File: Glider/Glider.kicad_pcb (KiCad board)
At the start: 2 copper layers, 100 x 200 mm, 3 parts

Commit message: Glider done !
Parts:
- removed H3: Panel, Kosmo_panel:Kosmo_Panel_Dual_Mounting_Holes
- added C1: 100n, Capacitor_THT:C_Disc_D7.0mm_W2.5mm_P5.00mm, F.Cu at (28.7, 115.4)
- added C2: 100n, Capacitor_THT:C_Disc_D7.0mm_W2.5mm_P5.00mm, F.Cu at (20.7, 125.2)
- added C3: 470n, Capacitor_THT:C_Disc_D7.0mm_W2.5mm_P5.00mm, F.Cu at (35.3, 47.9)
- added C4: 470n, Capacitor_THT:C_Disc_D7.0mm_W2.5mm_P5.00mm, F.Cu at (35.4, 144.1)
- added D1: LED, LED_SMD:LED_1206_3216Metric_ReverseMount_Hole1.8x2.4mm, B.Cu at (29.9, 91.2)
- added D2: 1N4148, Diode_THT:D_DO-35_SOD27_P7.62mm_Horizontal, F.Cu at (21.8, 51.9)
- added D3: 1N4148, Diode_THT:D_DO-35_SOD27_P7.62mm_Horizontal, F.Cu at (17.2, 49.1)
- added D4: LED, LED_SMD:LED_1206_3216Metric_ReverseMount_Hole1.8x2.4mm, B.Cu at (30.1, 185.4)
- added D5: 1N4148, Diode_THT:D_DO-35_SOD27_P7.62mm_Horizontal, F.Cu at (22.0, 148.3)
- added D6: 1N4148, Diode_THT:D_DO-35_SOD27_P7.62mm_Horizontal, F.Cu at (17.2, 145.6)
- added J1: EuroPower, telec:EuroPower, B.Cu at (29.7, 25.8)
- added J2: OUT1, telec:JackHole, F.Cu at (23.3, 101.9)
- added J3: IN1, telec:JackHole, F.Cu at (23.3, 80.9)
- added J4: OUT2, telec:JackHole, F.Cu at (23.3, 196.1)
- added J5: IN2, telec:JackHole, F.Cu at (23.3, 175.1)
- added LOGO1: telec, logo:telec-8, F.Cu at (25.0, 16.4)
- added R1: 2k2, Resistor_SMD:R_1206_3216Metric_Pad1.42x1.75mm_HandSolder, B.Cu at (32.8, 109.8)
- added R2: 1k, Resistor_THT:R_Axial_DIN0204_L3.6mm_D1.6mm_P7.62mm_Horizontal, F.Cu at (36.0, 93.0)
- added R3: 100, Resistor_THT:R_Axial_DIN0204_L3.6mm_D1.6mm_P7.62mm_Horizontal, F.Cu at (32.4, 53.2)
- added R4: 2k2, Resistor_SMD:R_1206_3216Metric_Pad1.42x1.75mm_HandSolder, B.Cu at (34.5, 182.9)
- added R5: 1k, Resistor_THT:R_Axial_DIN0204_L3.6mm_D1.6mm_P7.62mm_Horizontal, F.Cu at (36.0, 187.2)
- added R6: 100, Resistor_THT:R_Axial_DIN0204_L3.6mm_D1.6mm_P7.62mm_Horizontal, F.Cu at (32.7, 149.4)
- added RV1: 1M, Potentiometer_THT:Potentiometer_Alps_RK09K_Single_Vertical, F.Cu at (27.1, 45.6)
- added RV2: 1M, Potentiometer_THT:Potentiometer_Alps_RK09K_Single_Vertical, F.Cu at (27.1, 141.7)
- added SW1: LIN/LOG, telec:SW_L13.2mm_W7.9mm_P4.7mm, F.Cu at (32.3, 61.5)
- added SW2: UP/DOWN, telec:SW_L13.2mm_W7.9mm_P4.7mm, F.Cu at (16.9, 61.6)
- added SW3: LIN/LOG, telec:SW_L13.2mm_W7.9mm_P4.7mm, F.Cu at (32.1, 157.7)
- added SW4: UP/DOWN, telec:SW_L13.2mm_W7.9mm_P4.7mm, F.Cu at (17.0, 157.7)
- added U1: TL082, Package_DIP:DIP-8_W7.62mm_LongPads, F.Cu at (14.5, 114.3)
- added U2: TL082, Package_DIP:DIP-8_W7.62mm_LongPads, F.Cu at (27.2, 118.7)
- H1, H2: value Panel -> Mounting_Holes
- moved H2 47.6 mm to (15.1, 209.1)
- moved H1 19.0 mm to (34.1, 209.1)
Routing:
- net -12V: track 0.00 -> 132.7 mm
- net +12V: track 0.00 -> 132.7 mm
- net Net-(C3-Pad2): track 0.00 -> 109.2 mm
- net Net-(R3-Pad1): track 0.00 -> 75.0 mm
- net Net-(J4-PadT): track 0.00 -> 71.7 mm, vias 0 -> 1
- net /OUT2: track 0.00 -> 69.4 mm, vias 0 -> 1
- net Net-(SW1-Pad2): track 0.00 -> 68.9 mm
- net /IN1: track 0.00 -> 66.8 mm
- net Net-(C4-Pad2): track 0.00 -> 58.2 mm
- net /IN2: track 0.00 -> 51.7 mm
- net Net-(R6-Pad1): track 0.00 -> 50.7 mm
- net Net-(SW3-Pad2): track 0.00 -> 46.6 mm
- net Net-(J2-PadT): track 0.00 -> 38.9 mm
- net Net-(R6-Pad2): track 0.00 -> 30.2 mm
- net Net-(R3-Pad2): track 0.00 -> 30.1 mm
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- added copper zone on B.Cu, net GND
- added copper zone on F.Cu, net GND
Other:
- board size 100 x 200 mm -> 25 x 200 mm
- board text added: "+12V"
- board text added: "-12V"
- board text added: "DOWN"
- board text added: "Dual CV Glider"
- board text added: "From Harald Antes schematic, from Ives Uson"
- board text added: "GND"
- board text added: "LIN/LOG"
- board text added: "UP"

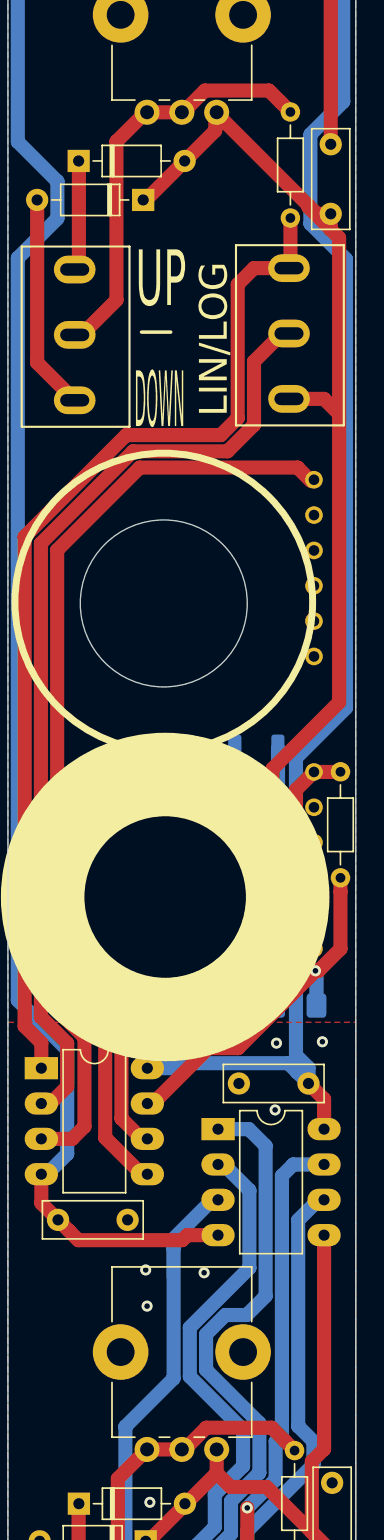
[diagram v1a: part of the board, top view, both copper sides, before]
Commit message: Changed pot direction
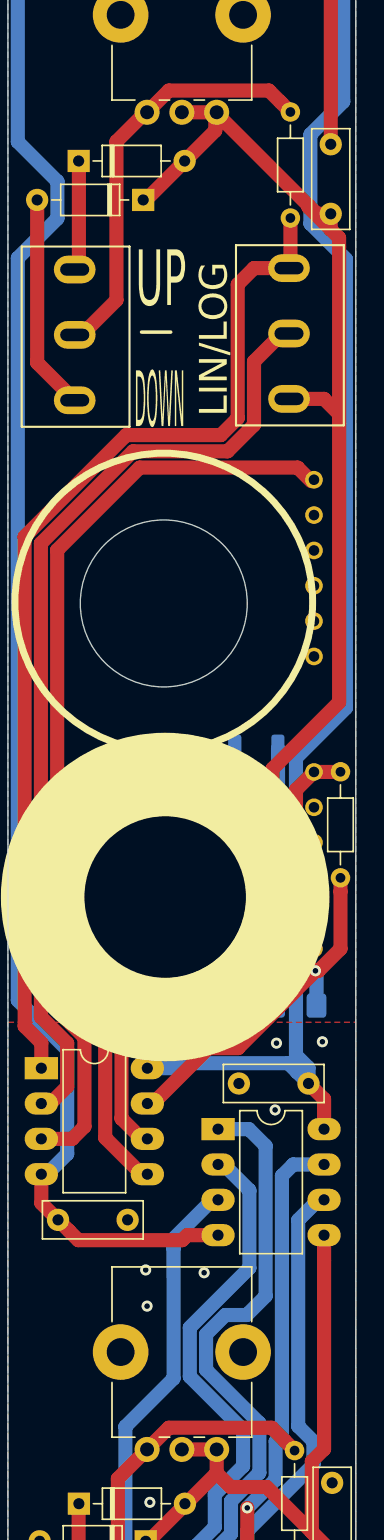
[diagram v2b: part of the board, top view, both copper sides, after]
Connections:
- RV1 pad 2: Net-(R3-Pad2) -> Net-(C3-Pad2)
- RV2 pad 2: Net-(R6-Pad2) -> Net-(C4-Pad2)
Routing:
- net Net-(C4-Pad2): track 58.2 -> 60.9 mm
- net Net-(C3-Pad2): track 109.2 -> 111.9 mm
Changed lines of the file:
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@@
   )
   (setup
-    (last_trace_width 0.1524)
+    (last_trace_width 1.016)
     (user_trace_width 0.1524)
     (user_trace_width 0.254)
@@
       (net 4 "Net-(C3-Pad2)"))
     (pad 2 thru_hole circle (at 0 -2.5 90) (size 1.8 1.8) (drill 1) (layers *.Cu *.Mask)
-      (net 26 "Net-(R3-Pad2)"))
+      (net 4 "Net-(C3-Pad2)"))
     (pad 3 thru_hole circle (at 0 -5 90) (size 1.8 1.8) (drill 1) (layers *.Cu *.Mask)
       (net 26 "Net-(R3-Pad2)"))
@@
       (net 5 "Net-(C4-Pad2)"))
     (pad 2 thru_hole circle (at 0 -2.5 90) (size 1.8 1.8) (drill 1) (layers *.Cu *.Mask)
-      (net 35 "Net-(R6-Pad2)"))
+      (net 5 "Net-(C4-Pad2)"))
     (pad 3 thru_hole circle (at 0 -5 90) (size 1.8 1.8) (drill 1) (layers *.Cu *.Mask)
       (net 35 "Net-(R6-Pad2)"))
@@
   (segment (start 29.3 148.73159) (end 28.13159 149.9) (width 1.016) (layer B.Cu) (net 21))
   (segment (start 29.3 147.55238) (end 29.3 148.73159) (width 1.016) (layer B.Cu) (net 21))
-  (segment (start 22 45.6) (end 24.5 45.6) (width 1.016) (layer F.Cu) (net 26))
   (segment (start 17.4 61.6) (end 19.9 59.1) (width 1.016) (layer F.Cu) (net 26))
   (segment (start 16.9 61.6) (end 17.4 61.6) (width 1.016) (layer F.Cu) (net 26))
   (segment (start 19.9 47.7) (end 22 45.6) (width 1.016) (layer F.Cu) (net 26))
   (segment (start 19.9 59.1) (end 19.9 47.7) (width 1.016) (layer F.Cu) (net 26))
+  (segment (start 24.5 45.6) (end 24.690606 45.6) (width 1.016) (layer F.Cu) (net 4))
+  (segment (start 24.6 45.6) (end 27.1 45.6) (width 1.016) (layer F.Cu) (net 4))
   (segment (start 31.700001 44.880001) (end 32.4 45.58) (width 1.016) (layer F.Cu) (net 26))
+  (segment (start 22.1 45.6) (end 23.660401 44.039599) (width 1.016) (layer F.Cu) (net 26))
   (segment (start 30.859599 44.039599) (end 31.700001 44.880001) (width 1.016) (layer F.Cu) (net 26))
-  (segment (start 26.251007 44.039599) (end 30.859599 44.039599) (width 1.016) (layer F.Cu) (net 26))
-  (segment (start 24.5 45.6) (end 24.690606 45.6) (width 1.016) (layer F.Cu) (net 26))
-  (segment (start 24.690606 45.6) (end 26.251007 44.039599) (width 1.016) (layer F.Cu) (net 26))
+  (segment (start 23.660401 44.039599) (end 30.859599 44.039599) (width 1.016) (layer F.Cu) (net 26))
   (segment (start 31.8 61.5) (end 32.3 61.5) (width 1.016) (layer F.Cu) (net 27))
   (segment (start 29.784 63.516) (end 31.8 61.5) (width 1.016) (layer F.Cu) (net 27))
@@
   (segment (start 20 155) (end 20 143.8) (width 1.016) (layer F.Cu) (net 35))
   (segment (start 17.3 157.7) (end 20 155) (width 1.016) (layer F.Cu) (net 35))
-  (segment (start 22.1 141.7) (end 24.6 141.7) (width 1.016) (layer F.Cu) (net 35))
+  (segment (start 24.6 141.7) (end 27.1 141.7) (width 1.016) (layer F.Cu) (net 5))
+  (segment (start 24.6 141.7) (end 24.790606 141.7) (width 1.016) (layer F.Cu) (net 5))
+  (segment (start 31.059599 140.139599) (end 32.000001 141.080001) (width 1.016) (layer F.Cu) (net 35))
+  (segment (start 22.1 141.7) (end 23.660401 140.139599) (width 1.016) (layer F.Cu) (net 35))
   (segment (start 32.000001 141.080001) (end 32.7 141.78) (width 1.016) (layer F.Cu) (net 35))
-  (segment (start 31.059599 140.139599) (end 32.000001 141.080001) (width 1.016) (layer F.Cu) (net 35))
-  (segment (start 26.351007 140.139599) (end 31.059599 140.139599) (width 1.016) (layer F.Cu) (net 35))
-  (segment (start 24.6 141.7) (end 24.790606 141.7) (width 1.016) (layer F.Cu) (net 35))
-  (segment (start 24.790606 141.7) (end 26.351007 140.139599) (width 1.016) (layer F.Cu) (net 35))
+  (segment (start 23.660401 140.139599) (end 31.059599 140.139599) (width 1.016) (layer F.Cu) (net 35))
   (segment (start 32.7 152.401) (end 32.1 153.001) (width 1.016) (layer F.Cu) (net 36))
   (segment (start 32.7 149.4) (end 32.7 152.401) (width 1.016) (layer F.Cu) (net 36))

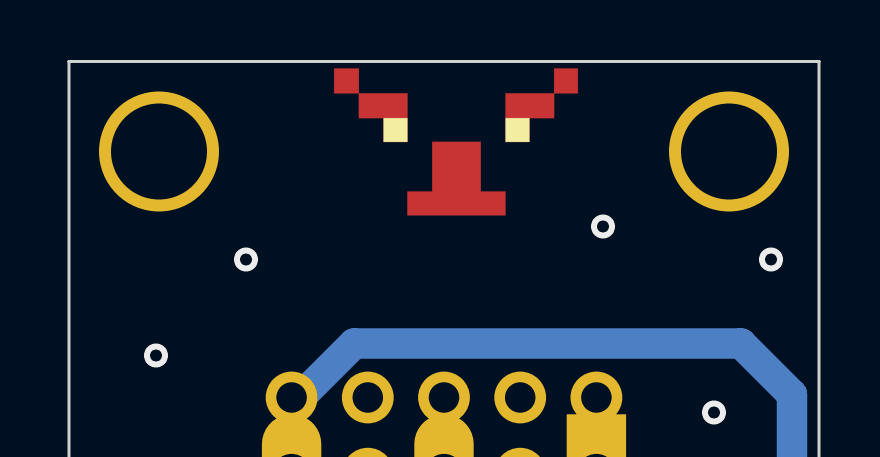
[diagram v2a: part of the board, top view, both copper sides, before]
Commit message: Added PCB ref stamp and send to prod!
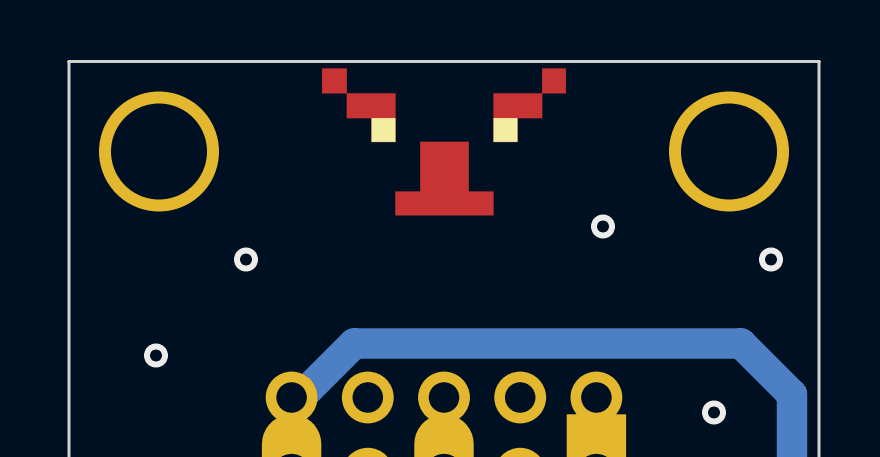
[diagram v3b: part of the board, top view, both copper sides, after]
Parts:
- moved LOGO1 0.40 mm to (24.6, 16.4)
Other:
- board text added: "PCB ref here:"
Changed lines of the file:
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@@
   (general
     (thickness 1.6)
-    (drawings 47)
+    (drawings 52)
     (tracks 267)
     (zones 0)
@@
   )
   (setup
-    (last_trace_width 1.016)
+    (last_trace_width 0.1524)
     (user_trace_width 0.1524)
     (user_trace_width 0.254)
@@
   )
   (module logo:telec-8 (layer F.Cu)
-    (at 25 16.4)
+    (at 24.6 16.4)
     (fp_text reference LOGO1 (at 0 0) (layer F.SilkS) hide
       (effects (font (size 1.524 1.524) (thickness 0.3)))
@@
       (net 1 GND))
     (pad "" np_thru_hole circle (at 0 0 90) (size 12 12) (drill 12) (layers *.Cu *.Mask))
+  )
+  (gr_line (start 30.4 12.1) (end 19 12.1) (layer B.SilkS) (width 0.15))
+  (gr_line (start 30.4 16.4) (end 30.4 12.1) (layer B.SilkS) (width 0.15))
+  (gr_line (start 19 16.4) (end 30.4 16.4) (layer B.SilkS) (width 0.15))
+  (gr_line (start 19 12.1) (end 19 16.4) (layer B.SilkS) (width 0.15))
+  (gr_text "PCB ref here:" (at 24.6 13) (layer B.SilkS)
+    (effects (font (size 1 1) (thickness 0.15)) (justify mirror))
   )
   (gr_text "From Harald Antes schematic,\nfrom Ives Uson" (at 24.9 206.9) (layer B.SilkS)
@@
   (segment (start 33.7 52.3) (end 34.3 52.9) (width 1.016) (layer F.Cu) (net 4))
   (segment (start 27 45.6) (end 33.7 52.3) (width 1.016) (layer F.Cu) (net 4))
+  (segment (start 24.5 45.6) (end 24.690606 45.6) (width 1.016) (layer F.Cu) (net 4))
+  (segment (start 24.6 45.6) (end 27.1 45.6) (width 1.016) (layer F.Cu) (net 4))
   (segment (start 22.2 148.3) (end 24.8 145.7) (width 1.016) (layer F.Cu) (net 5))
   (segment (start 22.02 148.3) (end 22.2 148.3) (width 1.016) (layer F.Cu) (net 5))
@@
   (segment (start 35.4 149.1) (end 33.939599 147.639599) (width 1.016) (layer F.Cu) (net 5))
   (segment (start 33.939599 147.639599) (end 33.939599 142.553795) (width 1.016) (layer F.Cu) (net 5))
+  (segment (start 24.6 141.7) (end 27.1 141.7) (width 1.016) (layer F.Cu) (net 5))
+  (segment (start 24.6 141.7) (end 24.790606 141.7) (width 1.016) (layer F.Cu) (net 5))
   (segment (start 14.2 51.9) (end 14.2 63.5) (width 1.016) (layer F.Cu) (net 6))
   (segment (start 16.9 66.299) (end 16.899 66.299) (width 1.016) (layer F.Cu) (net 6))
@@
   (segment (start 19.9 47.7) (end 22 45.6) (width 1.016) (layer F.Cu) (net 26))
   (segment (start 19.9 59.1) (end 19.9 47.7) (width 1.016) (layer F.Cu) (net 26))
-  (segment (start 24.5 45.6) (end 24.690606 45.6) (width 1.016) (layer F.Cu) (net 4))
-  (segment (start 24.6 45.6) (end 27.1 45.6) (width 1.016) (layer F.Cu) (net 4))
   (segment (start 31.700001 44.880001) (end 32.4 45.58) (width 1.016) (layer F.Cu) (net 26))
   (segment (start 22.1 45.6) (end 23.660401 44.039599) (width 1.016) (layer F.Cu) (net 26))
@@
   (segment (start 20 155) (end 20 143.8) (width 1.016) (layer F.Cu) (net 35))
   (segment (start 17.3 157.7) (end 20 155) (width 1.016) (layer F.Cu) (net 35))
-  (segment (start 24.6 141.7) (end 27.1 141.7) (width 1.016) (layer F.Cu) (net 5))
-  (segment (start 24.6 141.7) (end 24.790606 141.7) (width 1.016) (layer F.Cu) (net 5))
   (segment (start 31.059599 140.139599) (end 32.000001 141.080001) (width 1.016) (layer F.Cu) (net 35))
   (segment (start 22.1 141.7) (end 23.660401 140.139599) (width 1.016) (layer F.Cu) (net 35))
@@
     (polygon
       (pts
-        (xy 29.1 20.5) (xy 20.9 20.5) (xy 20.9 12.3) (xy 29.1 12.3)
+        (xy 28.7 20.5) (xy 20.5 20.5) (xy 20.5 12.3) (xy 28.7 12.3)
       )
     )

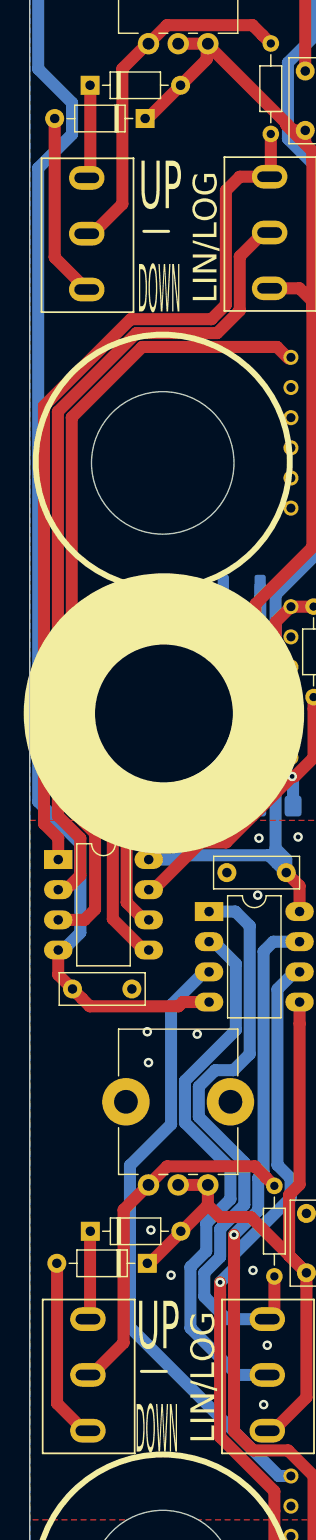
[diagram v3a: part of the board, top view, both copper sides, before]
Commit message: Analog modules finished
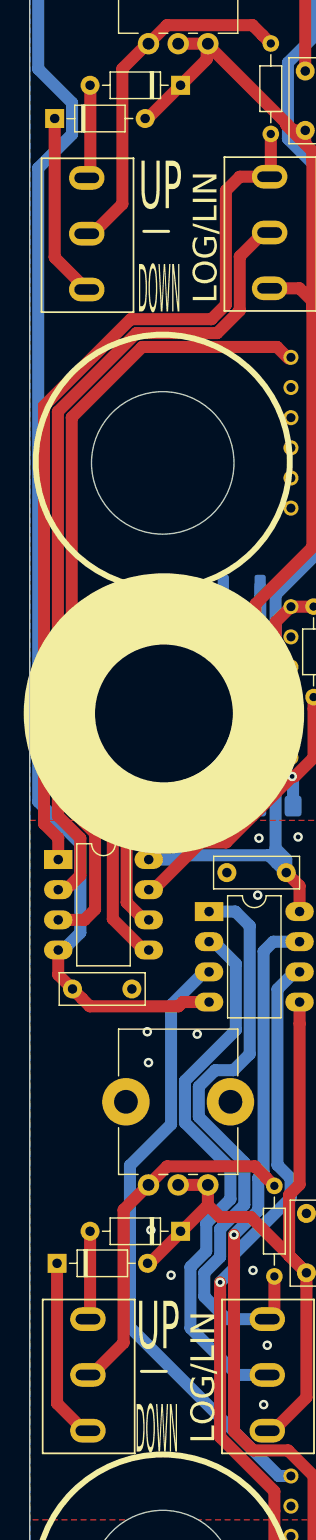
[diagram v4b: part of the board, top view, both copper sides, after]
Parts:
- moved D2 7.62 mm to (14.2, 51.9), turned to 0 degrees
- moved D3 7.62 mm to (24.8, 49.1), turned to 180 degrees
- moved D6 7.60 mm to (24.8, 145.6), turned to 180 degrees
- moved D5 7.60 mm to (14.4, 148.3), turned to 0 degrees
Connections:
- D2 pad 1: Net-(C3-Pad2) -> Net-(D2-Pad1)
- D2 pad 2: Net-(D2-Pad2) -> Net-(C3-Pad2)
- D3 pad 1: Net-(D3-Pad1) -> Net-(C3-Pad2)
- D3 pad 2: Net-(C3-Pad2) -> Net-(D3-Pad2)
- D5 pad 1: Net-(C4-Pad2) -> Net-(D5-Pad1)
- D5 pad 2: Net-(D5-Pad2) -> Net-(C4-Pad2)
- D6 pad 1: Net-(D6-Pad1) -> Net-(C4-Pad2)
- D6 pad 2: Net-(C4-Pad2) -> Net-(D6-Pad2)
- SW2 pad 1: Net-(D2-Pad2) -> Net-(D2-Pad1)
- SW2 pad 3: Net-(D3-Pad1) -> Net-(D3-Pad2)
- SW4 pad 1: Net-(D5-Pad2) -> Net-(D5-Pad1)
- SW4 pad 3: Net-(D6-Pad1) -> Net-(D6-Pad2)
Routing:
- net Net-(D2-Pad2): track 15.5 -> 0.00 mm
- net Net-(D2-Pad1): track 0.00 -> 15.5 mm
- net Net-(D5-Pad2): track 15.4 -> 0.00 mm
- net Net-(D5-Pad1): track 0.00 -> 15.4 mm
- net Net-(D3-Pad2): track 0.00 -> 7.93 mm
- net Net-(D3-Pad1): track 7.93 -> 0.00 mm
- net Net-(D6-Pad2): track 0.00 -> 7.38 mm
- net Net-(D6-Pad1): track 7.38 -> 0.00 mm
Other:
- board text added: "LOG/LIN"
- board text removed: "LIN/LOG"

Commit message: updated footprints on Glider
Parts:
- J2, J3, J4, J5: footprint telec:JackHole -> telec:Jack_Hole_Square
- moved R1 15.6 mm to (34.4, 94.3), turned to 135 degrees
- moved R2 5.09 mm to (35.7, 98.1)
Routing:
- net Net-(D1-Pad2): track 18.6 -> 2.74 mm
- net Net-(J4-PadT): track 71.7 -> 76.9 mm
- net /IN2: track 51.7 -> 55.7 mm
- net /OUT1: track 26.1 -> 29.9 mm, vias 1 -> 0
- net Net-(J2-PadT): track 38.9 -> 35.9 mm

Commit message: Prepared for release
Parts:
- moved R4 0.20 mm to (34.5, 182.7)
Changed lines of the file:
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@@
   )
   (setup
-    (last_trace_width 1.016)
+    (last_trace_width 0.1524)
     (user_trace_width 0.1524)
     (user_trace_width 0.254)
@@
   )
   (module Resistor_SMD:R_1206_3216Metric_Pad1.42x1.75mm_HandSolder (layer B.Cu)
-    (at 34.5125 182.9 180)
+    (at 34.5125 182.7 180)
     (descr "Resistor SMD 1206 (3216 Metric), square (rectangular) end terminal, IPC_7351 nominal with elongated pad for handsoldering. (Body size source: http://www.tortai-tech.com/upload/download/2011102023233369053.pdf), generated with kicad-footprint-generator")
     (tags "resistor handsolder")

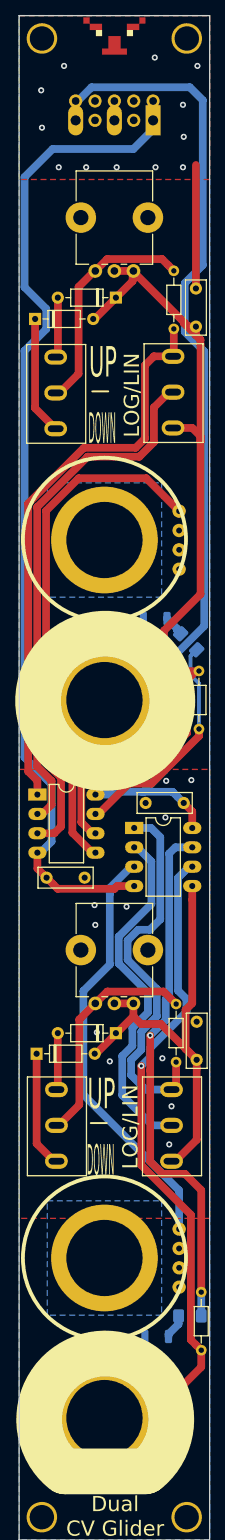
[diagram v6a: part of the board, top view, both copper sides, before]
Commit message: More clearance
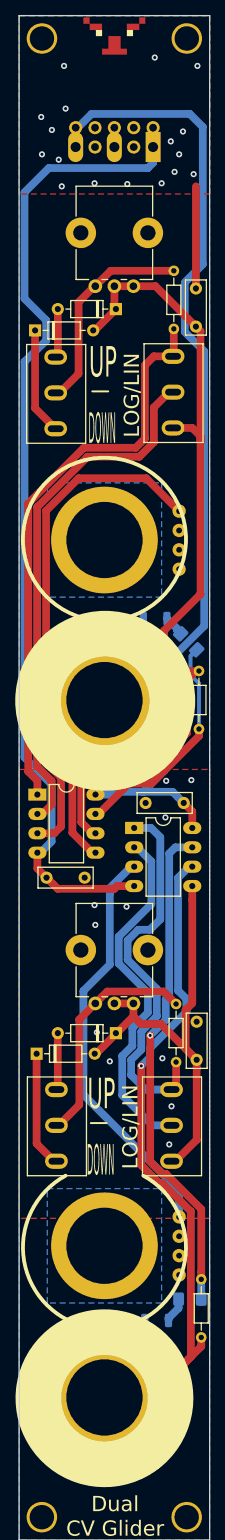
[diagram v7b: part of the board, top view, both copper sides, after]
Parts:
- moved J1 3.50 mm to (29.7, 29.3)
- moved J4 2.70 mm to (23.3, 193.4)
- moved R4 2.20 mm to (34.5, 180.5)
- moved D4 2.10 mm to (30.1, 183.3)
- moved RV1 2.00 mm to (27.1, 47.6)
- moved R5 1.68 mm to (36.0, 185.5)
- moved J5 1.60 mm to (23.3, 173.5)
- moved D2 1.50 mm to (14.2, 53.4)
- moved D3 1.50 mm to (24.8, 50.6)
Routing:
- net Net-(C3-Pad2): track 111.9 -> 107.2 mm
- net +12V: track 132.8 -> 129.2 mm
- net /OUT2: track 69.4 -> 66.2 mm
- net GND: track 16.2 -> 13.4 mm, vias 23 -> 28
- net Net-(R3-Pad2): track 30.0 -> 27.5 mm
- net Net-(J4-PadT): track 76.9 -> 78.7 mm
- net /IN2: track 55.7 -> 54.0 mm
- net Net-(D2-Pad1): track 15.5 -> 14.0 mm
- net Net-(D3-Pad2): track 7.93 -> 6.43 mm
- net -12V: track 132.7 -> 131.8 mm
